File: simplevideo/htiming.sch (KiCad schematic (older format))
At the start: 4 parts, among them U14 CD74HC40103, U15 CD74HC40103, U16 CD74HC40103, U17 74LS74

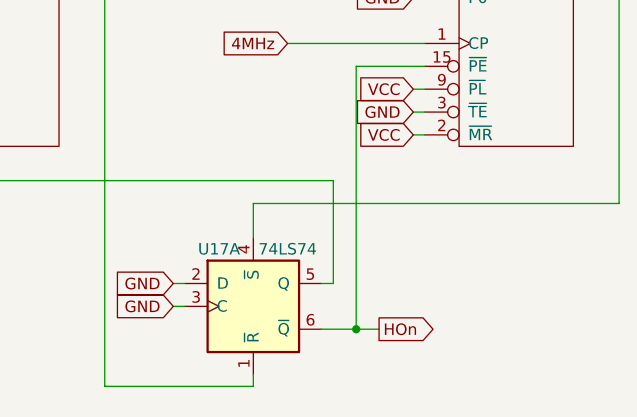
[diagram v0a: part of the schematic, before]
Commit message: Include 6502, ROM, etc in circuit, all laid out together
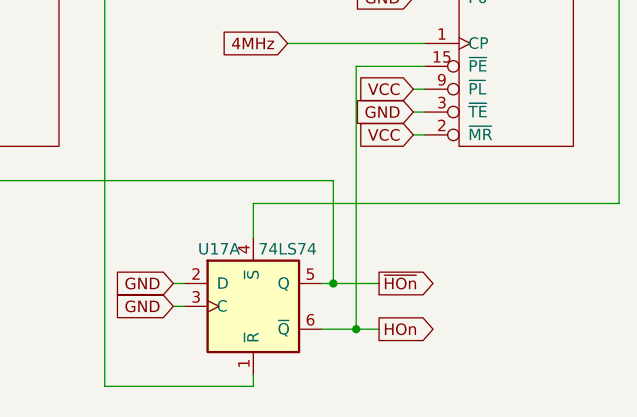
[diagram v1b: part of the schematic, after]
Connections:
- net ~HOn: now reaches U15.2 (~MR), U17.5 (Q)
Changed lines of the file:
@@
 $Descr A4 11693 8268
 encoding utf-8
-Sheet 4 5
+Sheet 4 7
 Title ""
 Date ""
@@
 	3700 2350 4300 2350
 NoConn ~ 2550 3400
+Text GLabel 6350 3200 2    50   Output ~ 0
+~HOn
+Wire Wire Line
+	6350 3200 6150 3200
+Connection ~ 6150 3200
 $EndSCHEMATC

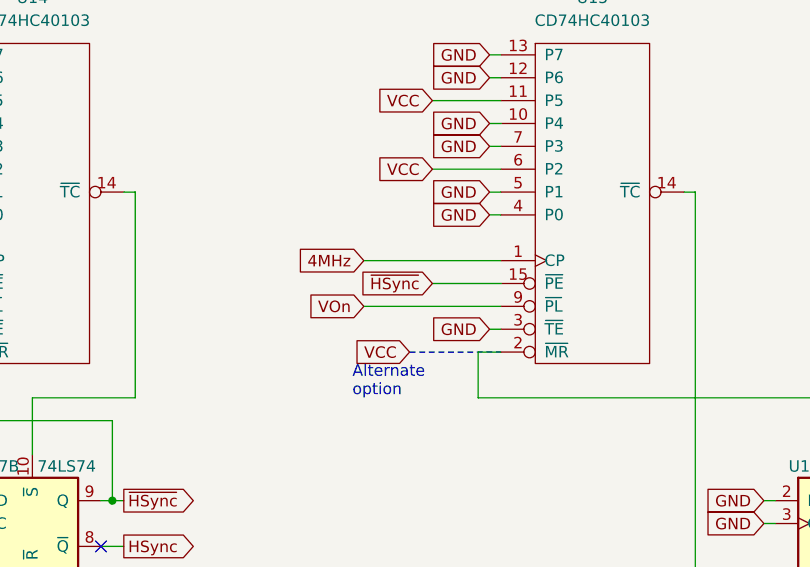
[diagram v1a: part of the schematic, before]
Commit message: New address decoding scheme and complete breadboard layout, should be ready to build
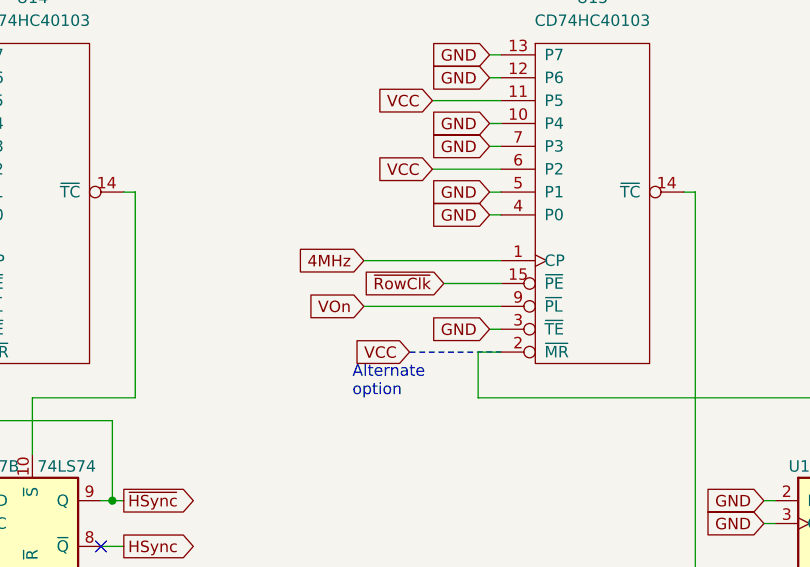
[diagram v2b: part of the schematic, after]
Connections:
- net ~HSync: no longer U15.15 (~PE)
- new net ~RowClk: U15.15 (~PE)
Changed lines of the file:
@@
 	5800 3650 5800 3600
 Wire Wire Line
-	4000 2250 4300 2250
+	4050 2250 4300 2250
 Text GLabel 2650 3200 2    50   Output ~ 0
 ~HSync
@@
 Text GLabel 3700 2350 0    50   Input ~ 0
 VOn
-Text GLabel 4000 2250 0    50   Input ~ 0
-~HSync
+Text GLabel 4050 2250 0    50   Input ~ 0
+~RowClk
 Wire Notes Line
 	3900 2550 4300 2550

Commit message: Fixed various issues discovered during building and testing
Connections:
- net ~RowClk is gone; now on net RowClk: U15.15 (~PE)
- net GND: now also U16.6 (P2); no longer U16.13 (P7)
- net VCC: now also U16.13 (P7); no longer U16.6 (P2)
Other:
- note added: "160 4MHz cycles"
- note added: "27 @6.75MHz"
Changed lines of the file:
@@
 Text GLabel 6250 1450 0    50   Input ~ 0
 VCC
-Text GLabel 6250 1750 0    50   Input ~ 0
-VCC
-Text GLabel 6500 1650 0    50   Input ~ 0
-GND
-Text GLabel 6500 1550 0    50   Input ~ 0
-GND
-Text GLabel 6500 1950 0    50   Input ~ 0
-GND
-Text GLabel 6500 1350 0    50   Input ~ 0
-GND
-Text GLabel 6500 1250 0    50   Input ~ 0
-GND
-Text GLabel 6500 1850 0    50   Input ~ 0
-GND
 Wire Wire Line
 	7400 1850 7400 2850
@@
 	6500 1850 6550 1850
 Wire Wire Line
-	6250 1750 6550 1750
+	6500 1750 6550 1750
 Wire Wire Line
 	6500 1650 6550 1650
@@
 	6500 1350 6550 1350
 Wire Wire Line
-	6500 1250 6550 1250
+	6250 1250 6550 1250
 Wire Wire Line
 	6550 1950 6500 1950
@@
 VOn
 Text GLabel 4050 2250 0    50   Input ~ 0
-~RowClk
+RowClk
 Wire Notes Line
 	3900 2550 4300 2550
@@
 	6350 3200 6150 3200
 Connection ~ 6150 3200
+Text Notes 650  1450 0    50   ~ 0
+27 @6.75MHz
+Text GLabel 6250 1250 0    50   Input ~ 0
+VCC
+Text GLabel 6500 1350 0    50   Input ~ 0
+GND
+Text GLabel 6500 1550 0    50   Input ~ 0
+GND
+Text GLabel 6500 1650 0    50   Input ~ 0
+GND
+Text GLabel 6500 1850 0    50   Input ~ 0
+GND
+Text GLabel 6500 1950 0    50   Input ~ 0
+GND
+Text GLabel 6500 1750 0    50   Input ~ 0
+GND
+Text Notes 5900 1150 0    50   ~ 0
+160 4MHz cycles
 $EndSCHEMATC
